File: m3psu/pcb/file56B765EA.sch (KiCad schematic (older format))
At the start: 0 parts

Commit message: Started work on the battery management sheet. Left half of MAX17435 is wired up.
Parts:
- added C? (x2): 2µ2, agg:0402, symbol C
- added C? (x2): 10p, agg:0402, symbol C
- added C? (x5): 100n, agg:0402, symbol C
- added C?: 1µ, agg:0402, symbol C
- added C?: 4µ7, agg:0402, symbol C
- added IC?: STM32F405RxTx, agg:LQFP-64, symbol STM32F405RxTx
- added R?: 100, agg:0402, symbol R
- added Y?: 26M, agg:XTAL-20x16, symbol SMD_XTAL
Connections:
- new net: C?.1, IC?.31 (VCAP_1)
- new net: C?.1, IC?.47 (VCAP_2)
- new net: C?.2, IC?.5 (PH0), Y?.1
- new net: IC?.6 (PH1), R?.2
- new net: C?.1, R?.1, Y?.3
- new net 3v3: C?.2, C?.2, C?.2, C?.2, C?.2, C?.2, C?.2, IC?.1 (VBAT), IC?.13 (VDDA), IC?.19 (VDD), IC?.32 (VDD), IC?.48 (VDD), IC?.64 (VDD)
- new net CAN_RXD: IC?.61 (PB8)
- new net CAN_TXD: IC?.62 (PB9)
- new net GND: C?.1, C?.1, C?.1, C?.1, C?.1, C?.1, C?.1, C?.1, C?.2, C?.2, C?.2, IC?.12 (VSSA), IC?.18 (VSS), IC?.60 (BOOT0), IC?.63 (VSS), Y?.2, Y?.4
- new net JTCK: IC?.49 (PA14)
- new net JTDI: IC?.50 (PA15)
- new net JTDO: IC?.55 (PB3)
- new net JTMS: IC?.46 (PA13)
- new net ~RST: IC?.7 (NRST)
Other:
- note added: "PB4 is JTRST, DO NOT CONNECT (Errata 2.1.4)"

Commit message: Changes in arrangement of schematic. Started wiring interconnects. WIP.
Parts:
- added IC?: MCP2562, agg:DFN-8-EP-MICROCHIP, symbol MCP2562
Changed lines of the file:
@@
 $Descr A4 11693 8268
 encoding utf-8
-Sheet 2 12
+Sheet 2 13
 Title ""
 Date ""
@@
 Comment4 ""
 $EndDescr
-Text Label 4900 5400 2    60   ~ 0
-JTDI
-Text Label 6100 2200 0    60   ~ 0
-JTDO
 Text Notes 6050 2300 0    60   ~ 0
 PB4 is JTRST, DO NOT CONNECT (Errata 2.1.4)
@@
 Wire Wire Line
 	5000 3700 4950 3700
-Text Label 6100 2800 0    60   ~ 0
-CAN_TXD
-Text Label 6100 2700 0    60   ~ 0
-CAN_RXD
 Wire Wire Line
 	6100 2800 6000 2800
@@
 Wire Wire Line
 	4800 3600 5000 3600
-Text Label 4900 5300 2    60   ~ 0
-JTCK
-Text Label 4900 5200 2    60   ~ 0
-JTMS
 $Comp
 L STM32F405RxTx IC?
@@
 	1    0    0    -1
 $EndComp
+Text HLabel 6100 2700 2    60   BiDi ~ 0
+CAN_RXD
+Text HLabel 6100 2800 2    60   BiDi ~ 0
+CAN_TXD
+Text HLabel 6100 2200 2    60   BiDi ~ 0
+JTDO
+Text HLabel 4900 5200 0    60   BiDi ~ 0
+JTMS
+Text HLabel 4900 5300 0    60   BiDi ~ 0
+JTCK
+Text HLabel 4900 5400 0    60   BiDi ~ 0
+JTDI
+$Comp
+L MCP2562 IC?
+U 1 1 56DF4FA9
+P 7600 2900
+F 0 "IC?" H 7300 3200 50  0000 L CNN
+F 1 "MCP2562" H 7300 2600 50  0000 L CNN
+F 2 "agg:DFN-8-EP-MICROCHIP" H 7300 2500 50  0001 L CNN
+F 3 "http://ww1.microchip.com/downloads/en/DeviceDoc/20005167C.pdf" H 7300 2400 50  0001 L CNN
+F 4 "" H 7300 2300 50  0001 L CNN "Farnell"
+F 5 "824-3135" H 7300 2200 50  0001 L CNN "RS"
+	1    7600 2900
+	1    0    0    -1
+$EndComp
+$Comp
+L VCC #PWR?
+U 1 1 56DF5743
+P 3650 900
+F 0 "#PWR?" H 3650 1010 50  0001 L CNN
+F 1 "VCC" H 3650 990 50  0000 C CNN
+F 2 "" H 3650 900 60  0000 C CNN
+F 3 "" H 3650 900 60  0000 C CNN
+	1    3650 900
+	1    0    0    -1
+$EndComp

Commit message: Grouped components, sorted internal interconnects. Sheets size now roughly proportional to number of components inside.
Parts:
- added C? (x2): 100n, agg:0402, symbol C
- added C?: 22n, ag:0402, symbol C
- added C?: 22n, agg:0402, symbol C
- added IC?: LTC4151, agg:DFN-10-EP-LT, symbol LTC4151
- added IC?: LTC4353, agg:DFN-16-EP-LTC-DE, symbol LTC4353
- added J?: WEST TOP, symbol CONN_02x10
- added J?: EAST TOP, symbol CONN_02x10
- added J?: WEST BOT, symbol CONN_02x10
- added J?: EAST BOT, symbol CONN_02x10
- added J?: NORTH TOP, symbol CONN_02x05
- added J?: NORTH BOT, symbol CONN_02x05
- added P?: SWD_TC, agg:TC2030-NL, symbol SWD_TC
- added Q? (x5): NFET, symbol NFET
- added Q? (x2): PFET, symbol PFET
- added R? (x2): 4k7, agg:0402, symbol R
- added R? (x2): 33k, agg:0402, symbol R
- added R?: 10m, agg:0805, symbol R
- added R? (x2): 47, agg:0805, symbol R
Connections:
- net 3v3: now also IC?.5 (VIO), P?.1 (VDD), R?.1, R?.1
- net CAN_RXD: now also IC?.4 (RXD)
- net CAN_TXD: now also IC?.1 (TXD)
- net GND: now also IC?.2 (VSS), IC?.8 (STBY), IC?.EP (VSS), C?.2, C?.2, IC?.15 (GND), IC?.3 (ADR1), IC?.4 (ADR0), IC?.5 (ADIN), IC?.9 (GND), IC?.EP (GND), IC?.EP (GND), J?.1, J?.1, J?.1, J?.1, J?.19, J?.19, J?.19, J?.19, J?.2, J?.2, J?.2, J?.2, J?.20, J?.20, J?.20, J?.20, P?.5 (GND), Q?.2 (S), Q?.2 (S), Q?.2 (S)
- net JTCK: now also J?.6, J?.6, P?.4 (SWDCLK)
- net JTDI: now also J?.8
- net JTDO: now also J?.8
- net JTMS: now also J?.4, J?.4, P?.2 (SWDIO)
- net VCC: now also IC?.1 (SENSE+), IC?.10 (OUT1), IC?.2 (VIN), IC?.7 (OUT2), J?.1, J?.1, J?.2, J?.2, Q?.2 (S), Q?.3 (D), R?.1, R?.1
- net ~RST: now also P?.3 (~RST)
- net 5v_CAN: now reaches IC?.3 (VDD)
- net 5v_CAN: now also C?.1, J?.14, J?.14
- net CAN-: now reaches IC?.6 (CANL)
- net CAN-: now also J?.16, J?.16
- net CAN+: now reaches IC?.7 (CANH)
- net CAN+: now also J?.18, J?.18
- new net: Q?.1 (G), Q?.3 (D), R?.2 (x2)
- new net: IC?.10 (SENSE-), Q?.2 (S), R?.2
- new net: Q?.2 (S), R?.2
- new net: Q?.3 (D), R?.2
- new net: C?.1, IC?.11 (CPO1)
- new net: IC?.12 (GATE1), Q?.1 (G)
- new net: C?.1, IC?.14 (VCC)
- new net: IC?.5 (GATE2), Q?.1 (G)
- new net: C?.1, IC?.6 (CPO2)
- new net 3v3_AUX1: J?.13, J?.13
- new net 3v3_AUX2: J?.15, J?.15
- new net 3v3_DL: J?.11, J?.11
- new net 3v3_FC: J?.7, J?.7
- new net 3v3_IMU: J?.3, J?.3
- new net 3v3_PSU: J?.3, J?.3
- new net 3v3_PYRO: J?.9, J?.9
- new net 3v3_RADIO: J?.5, J?.5
- new net 5v_AUX1: J?.11, J?.11
- new net 5v_AUX2: J?.13, J?.13
- new net 5v_CAM: J?.15, J?.15
- new net 5v_IMU: J?.9, J?.9
- new net 5v_RADIO: J?.7, J?.7
- new net BATT1: J?.6, J?.6, Q?.3 (D), R?.1
- new net BATT2: J?.8, J?.8, R?.1, R?.1
- new net BLEED_BATT1: Q?.1 (G)
- new net BLEED_BATT2: Q?.1 (G)
- new net CHARGE: C?.2, IC?.13 (VIN1), J?.17, J?.17, J?.18, J?.18, Q?.3 (D)
- new net EN_PYRO: Q?.1 (G)
- new net JTDR: J?.10, J?.10
- new net PWR: J?.16, J?.16
- new net PYRO1: J?.10, J?.10, J?.12, J?.12, J?.14, J?.14, J?.8, J?.8, Q?.3 (D)
- new net PYRO_SI: J?.5, J?.5, J?.6, J?.6
- new net PYRO_SO: J?.3, J?.3, J?.4, J?.4
- new net RSVD: J?.5, J?.5
- new net RSVD1: J?.12, J?.12
- new net RSVD2: J?.17, J?.17
- new net SCL: IC?.6 (SCL), J?.9, J?.9, R?.2
- new net SDA: IC?.7 (SDA), J?.7, J?.7, R?.2
- new net VBATT: C?.2, IC?.4 (VIN2), J?.4, J?.4, Q?.2 (S)
- new net ~ALERT: J?.10, J?.10
- new net ~EN_EXT_PWR: IC?.16 (~EN1)
- new net ~EN_INT_PWR: IC?.1 (~EN2)
- new net ~EXT_PWR_ON: IC?.9 (~ON_STAT1)
- new net ~INT_PWR_ON: IC?.8 (~ON_STAT2)
- no-connect marks 0 -> 3
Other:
- note added: "Address: 0x6F"
- note added: "INTERCONNECTS"
- note added: "PB4 is JTRST, NC (Errata 2.1.4)"
- note removed: "PB4 is JTRST, DO NOT CONNECT (Errata 2.1.4)"
- moved on the sheet: C?, IC?, R?, Y?

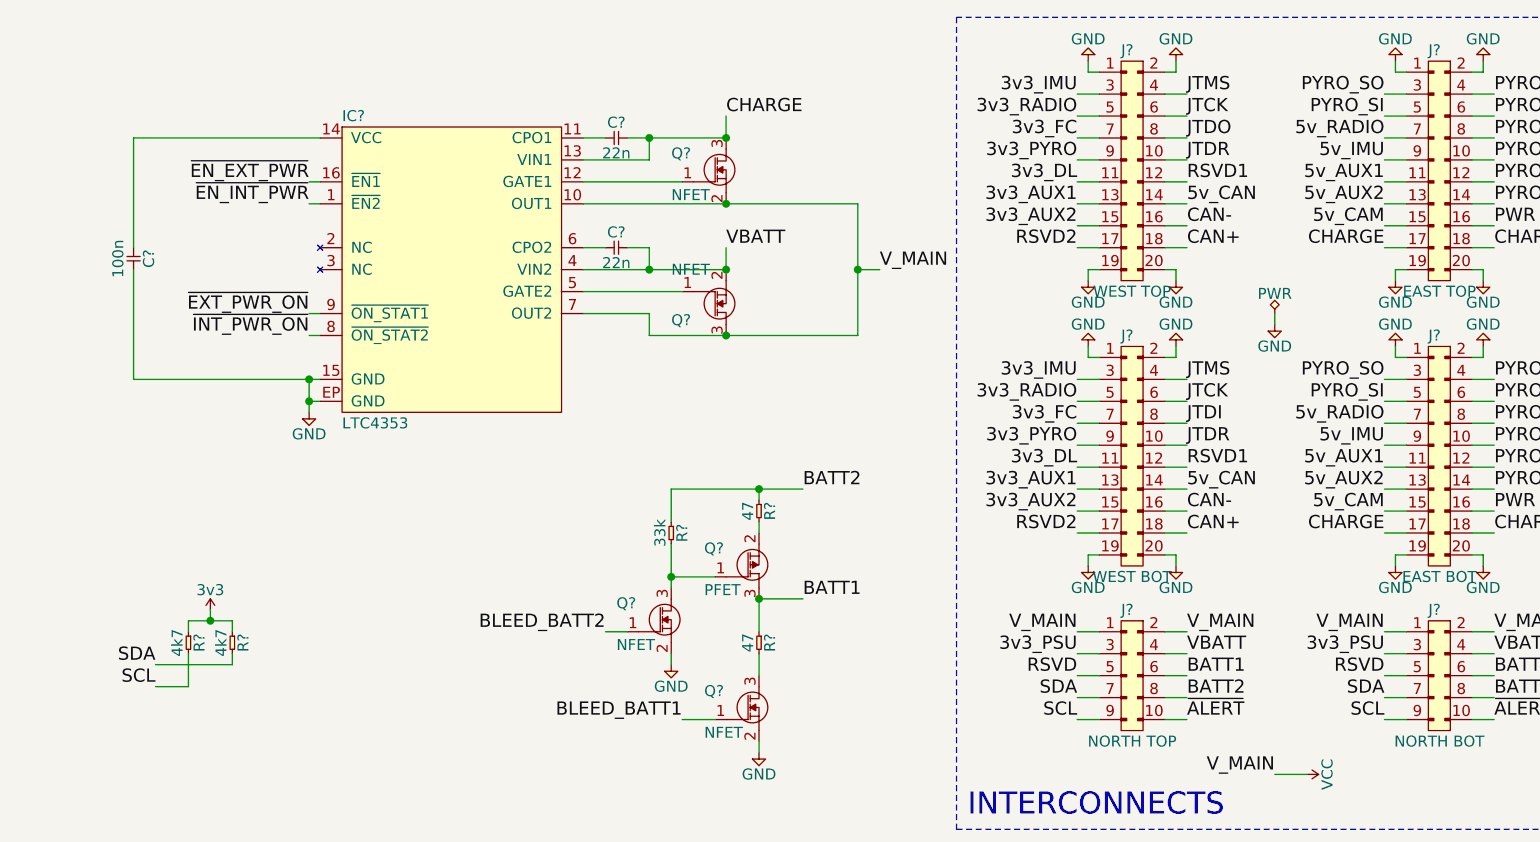
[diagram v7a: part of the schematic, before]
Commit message: Added footprints and datasheets to ALL transistors. Only 47uF capacitor has no footprint now.
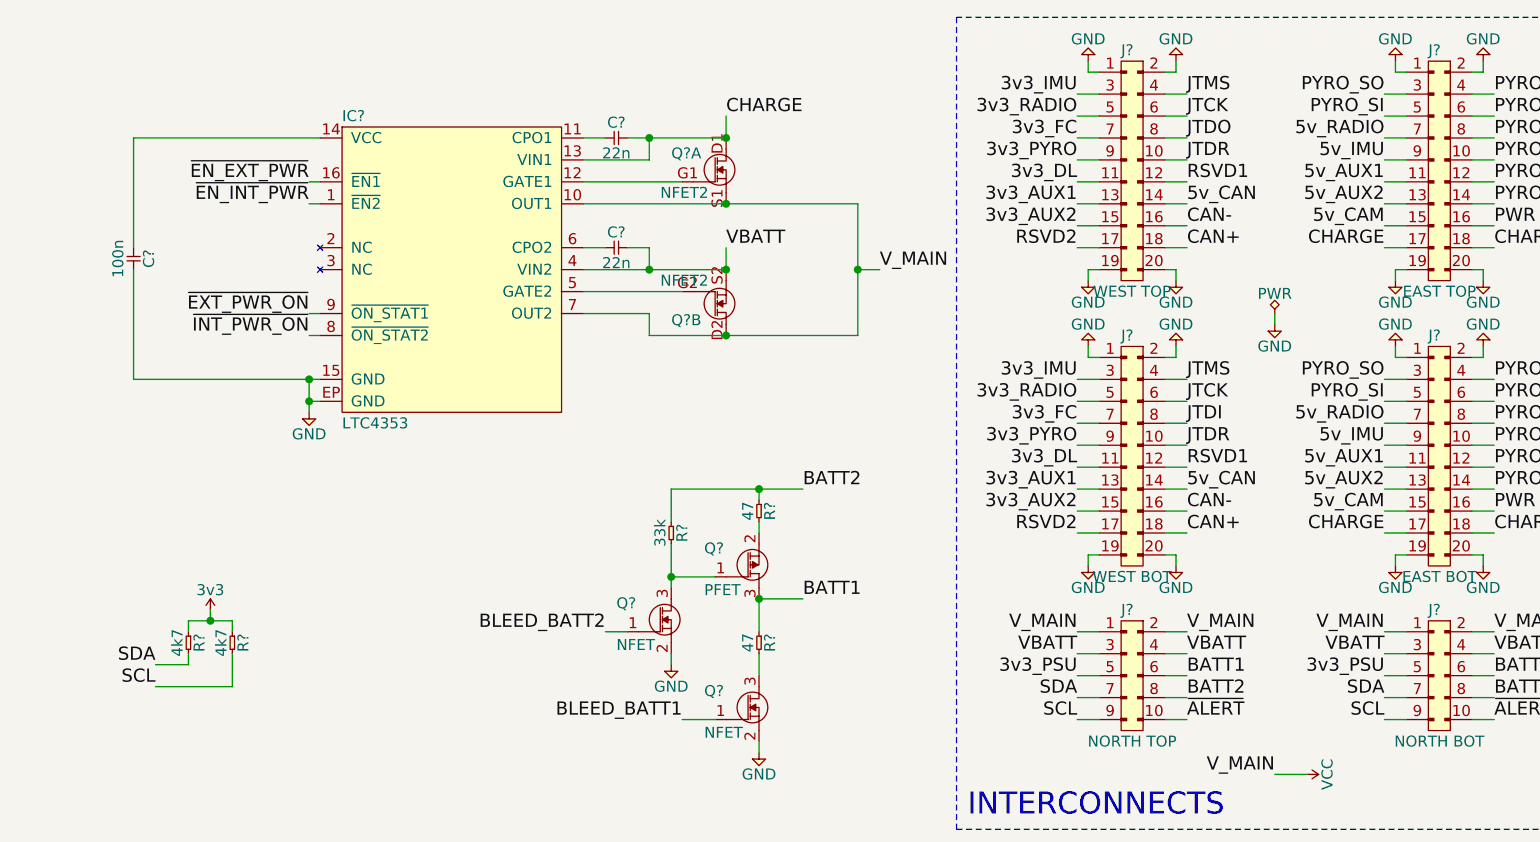
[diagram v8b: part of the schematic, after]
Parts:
- removed Q? (x2): NFET, symbol NFET
- added Q? (x2): NFET2, agg:PowerFLAT5x6, symbol NFET2
- Q? (x3): footprint (none) -> agg:VML1006
- Q?: footprint (none) -> SON2x2
- Q?: footprint (none) -> agg:PowerPAK-SC-75-6L-Single
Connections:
- net RSVD is gone; now on net 3v3_PSU: J?.5, J?.5
- net 3v3_PSU: no longer J?.3, J?.3
- net CHARGE: now also Q?.D1 (D)
- net SCL: now also R?.2; no longer R?.2
- net SDA: now also R?.2; no longer R?.2
- net VBATT: now also J?.3, J?.3, Q?.S2 (S)
- net VCC: now also Q?.D2 (D), Q?.S1 (S)
- net at IC?.12 (GATE1): now also Q?.G1 (G)
- net at IC?.5 (GATE2): now also Q?.G2 (G)
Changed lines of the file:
@@
 Text Label 4500 3600 2    60   ~ 0
 SCL
-Wire Wire Line
-	4500 3500 4850 3500
-Wire Wire Line
-	4500 3600 4650 3600
 $Comp
 L R R?
@@
 $EndComp
 Wire Wire Line
-	4850 3500 4850 3450
+	4850 3600 4850 3450
 $Comp
 L R R?
@@
 	4650 3300 4650 3350
 Wire Wire Line
-	4650 3600 4650 3450
+	4650 3500 4650 3450
 Wire Wire Line
 	4850 3300 4850 3350
@@
 F 0 "Q?" H 10050 5580 50  0000 L CNN
 F 1 "NFET" H 10050 5390 50  0000 L CNN
-F 2 "" H 10300 5550 50  0001 C CNN
-F 3 "" H 10300 5550 50  0001 C CNN
+F 2 "agg:VML1006" H 10300 5550 50  0001 C CNN
+F 3 "http://rohmfs.rohm.com/en/products/databook/datasheet/discrete/transistor/mosfet/rv2c010unt2l-e.pdf" H 10300 5550 50  0001 C CNN
 F 4 "2490619" H 10300 5550 60  0001 C CNN "Farnell"
 	1    10300 5550
@@
 F 0 "Q?" H 9700 5280 50  0000 L CNN
 F 1 "PFET" H 9700 5090 50  0000 L CNN
-F 2 "" H 9950 5250 50  0001 C CNN
-F 3 "" H 9950 5250 50  0001 C CNN
+F 2 "SON2x2" H 9950 5250 50  0001 C CNN
+F 3 "http://www.ti.com/lit/ds/symlink/csd25310q2.pdf" H 9950 5250 50  0001 C CNN
 F 4 "2501102" H 9950 5250 60  0001 C CNN "Farnell"
 	1    9950 5250
@@
 F 0 "Q?" H 7000 3030 50  0000 L CNN
 F 1 "PFET" H 7000 2840 50  0000 L CNN
-F 2 "" H 7250 3000 50  0001 C CNN
-F 3 "" H 7250 3000 50  0001 C CNN
+F 2 "agg:PowerPAK-SC-75-6L-Single" H 7250 3000 50  0001 C CNN
+F 3 "http://www.vishay.com/docs/65652/sib433ed.pdf" H 7250 3000 50  0001 C CNN
 F 4 "2335393" H 7250 3000 60  0001 C CNN "Farnell"
 	1    7250 3000
@@
 F 0 "Q?" H 7000 3680 50  0000 L CNN
 F 1 "NFET" H 7000 3490 50  0000 L CNN
-F 2 "" H 7250 3650 50  0001 C CNN
-F 3 "" H 7250 3650 50  0001 C CNN
+F 2 "agg:VML1006" H 7250 3650 50  0001 C CNN
+F 3 "http://rohmfs.rohm.com/en/products/databook/datasheet/discrete/transistor/mosfet/rv2c010unt2l-e.pdf" H 7250 3650 50  0001 C CNN
 F 4 "2490619" H 7250 3650 60  0001 C CNN "Farnell"
 	1    7250 3650
@@
 F 0 "Q?" H 6600 3280 50  0000 L CNN
 F 1 "NFET" H 6600 3090 50  0000 L CNN
-F 2 "" H 6850 3250 50  0001 C CNN
-F 3 "" H 6850 3250 50  0001 C CNN
+F 2 "agg:VML1006" H 6850 3250 50  0001 C CNN
+F 3 "http://rohmfs.rohm.com/en/products/databook/datasheet/discrete/transistor/mosfet/rv2c010unt2l-e.pdf" H 6850 3250 50  0001 C CNN
 F 4 "2490619" H 6850 3250 60  0001 C CNN "Farnell"
 	1    6850 3250
@@
 	1    5200 2350
 	1    0    0    -1
-$EndComp
-$Comp
-L NFET Q?
-U 1 1 56EA4D65
-P 7100 1200
-F 0 "Q?" H 6850 1230 50  0000 L CNN
-F 1 "NFET" H 6850 1040 50  0000 L CNN
-F 2 "" H 7100 1200 50  0001 C CNN
-F 3 "" H 7100 1200 50  0001 C CNN
-F 4 "2098274" H 7100 1200 60  0001 C CNN "Farnell"
-	1    7100 1200
-	1    0    0    -1
-$EndComp
-$Comp
-L NFET Q?
-U 1 1 56EA4D6D
-P 7100 1900
-F 0 "Q?" H 6850 1930 50  0000 L CNN
-F 1 "NFET" H 6850 1700 50  0000 L CNN
-F 2 "" H 7100 1900 50  0001 C CNN
-F 3 "" H 7100 1900 50  0001 C CNN
-F 4 "2098274" H 7100 1900 60  0001 C CNN "Farnell"
-	1    7100 1900
-	1    0    0    1
 $EndComp
 Wire Wire Line
@@
 SCL
 Text Label 8700 3450 2    60   ~ 0
-3v3_PSU
+VBATT
 Text Label 9200 3550 0    60   ~ 0
 BATT1
@@
 VBATT
 Text Label 8700 3550 2    60   ~ 0
-RSVD
+3v3_PSU
 Text Label 9200 3650 0    60   ~ 0
 BATT2
@@
 SCL
 Text Label 10100 3450 2    60   ~ 0
-3v3_PSU
+VBATT
 Text Label 10600 3550 0    60   ~ 0
 BATT1
@@
 VBATT
 Text Label 10100 3550 2    60   ~ 0
-RSVD
+3v3_PSU
 Text Label 10600 3650 0    60   ~ 0
 BATT2
@@
 Wire Wire Line
 	9600 4000 9750 4000
+$Comp
+L NFET2 Q?
+U 1 1 56E00BC6
+P 7100 1200
+F 0 "Q?" H 6850 1230 50  0000 L CNN
+F 1 "NFET2" H 6800 1050 50  0000 L CNN
+F 2 "agg:PowerFLAT5x6" H 7100 1200 50  0001 C CNN
+F 3 "http://www.st.com/web/en/resource/technical/document/datasheet/CD00279555.pdf" H 7100 1200 50  0001 C CNN
+F 4 "2098274" H 7100 1200 60  0001 C CNN "Farnell"
+	1    7100 1200
+	1    0    0    -1
+$EndComp
+$Comp
+L NFET2 Q?
+U 2 1 56E00C63
+P 7100 1900
+F 0 "Q?" H 6850 1930 50  0000 L CNN
+F 1 "NFET2" H 6800 1750 50  0000 L CNN
+F 2 "agg:PowerFLAT5x6" H 7100 1900 50  0001 C CNN
+F 3 "http://www.st.com/web/en/resource/technical/document/datasheet/CD00279555.pdf" H 7100 1900 50  0001 C CNN
+F 4 "2098274" H 7100 1900 60  0001 C CNN "Farnell"
+	2    7100 1900
+	1    0    0    1
+$EndComp
+Wire Wire Line
+	4650 3500 4500 3500
+Wire Wire Line
+	4500 3600 4850 3600
 $EndSCHEMATC
